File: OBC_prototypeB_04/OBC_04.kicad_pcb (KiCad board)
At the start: 2 copper layers, 95.9 x 90.2 mm, 108 parts, among them J1 PC104-8BIT, P1 3v3_IN_CONNECTOR, P10 FLASH_CS, P11 USB_5V, P12 LOAD, P13 WD_EN, P14 WD_RST_EN, P15 3pin-DC-power, P16 JTAG_10PIN, P2 INA_INPUT, P3 INA_GND, P4 INA_EN, P5 INA_OUTPUT, P6 USB_PORT, P8 RTC_SPI, P9 FLASH_SPI, Q1 DMN2075U, Q2 DMN2075U, Q3 1v2_GOOD, Q4 DMN2075U, Q5 DMN2075U, SW1 SPST, SW2 SPST, SW4 SPST, U1 TMS570LS0714, U10 FT230XQ-R, U11 STLM75, U2 XC6222B121MR-G, U3 AP7361_3.3v, U4 INA301, U5 FLASH_IS25LP016D, U6 FLASH_IS25LP016D, U7 FLASH_IS25LP016D, U8 AB-RTCMC-EOA9-S3, U9 TPS3110, Y1 XTAL

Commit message: Initial placement mostly complete
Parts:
- moved R22 159.0 mm to (68.5, 46.8)
- moved R23 159.0 mm to (68.1, 54.4)
- moved R25 148.4 mm to (73.0, 47.0)
- moved W14 142.8 mm to (89.0, 42.0)
- moved R24 131.7 mm to (71.0, 42.0)
- moved R36 130.9 mm to (70.0, 89.0)
- moved R37 130.4 mm to (68.0, 89.0)
- moved D4 127.3 mm to (73.5, 84.0)
- moved W12 127.1 mm to (78.0, 42.0)
- moved D5 126.3 mm to (70.5, 79.0)
- moved R32 125.7 mm to (66.5, 85.0)
- moved R33 125.7 mm to (69.5, 85.0)
- moved R34 125.7 mm to (66.5, 90.0)
- moved R7 123.3 mm to (158.4, 50.4)
- moved W7 119.2 mm to (153.6, 48.8)
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
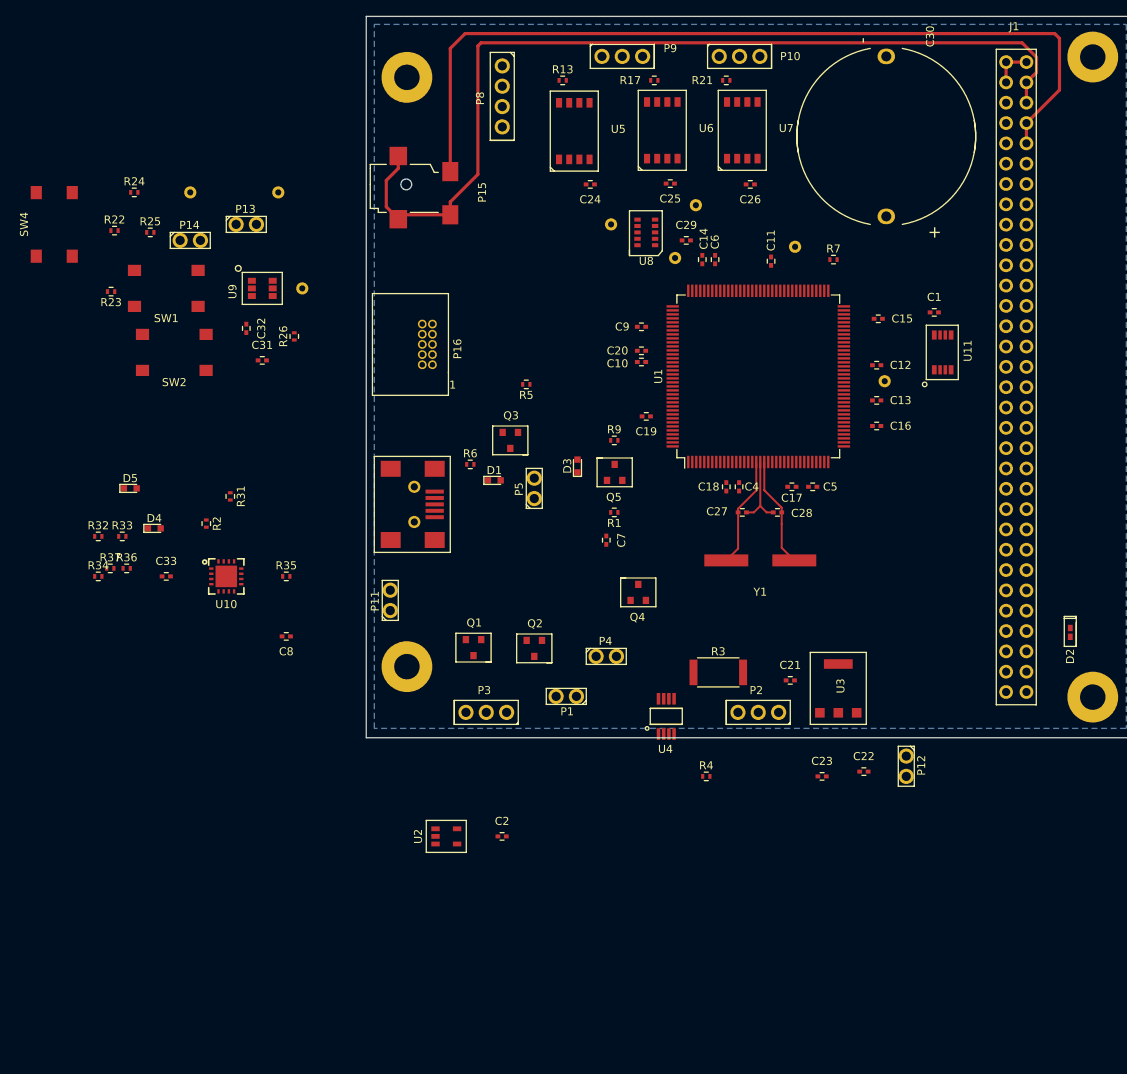
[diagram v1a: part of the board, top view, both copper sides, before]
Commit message: Routed USB, started reset area
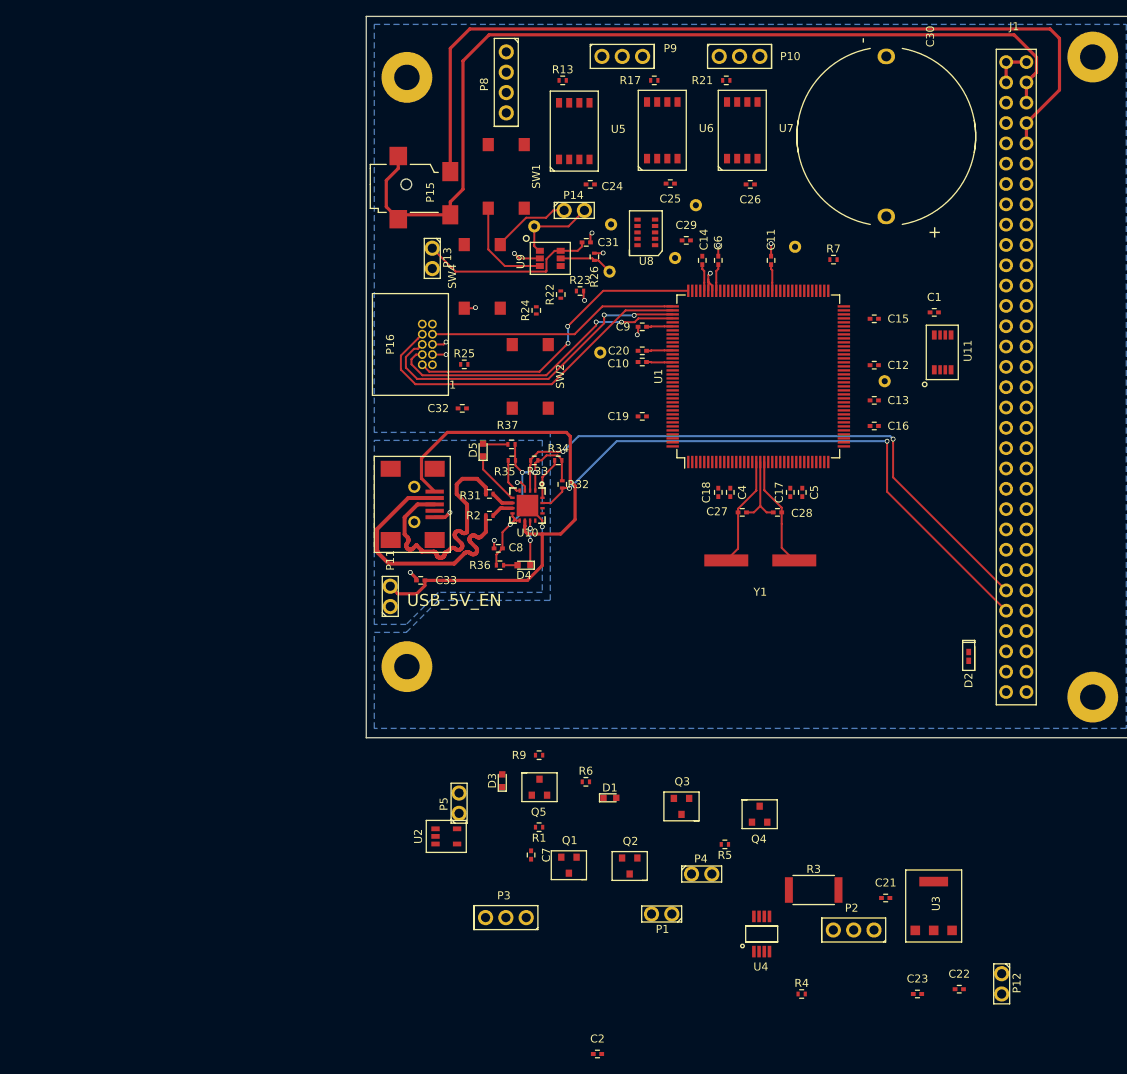
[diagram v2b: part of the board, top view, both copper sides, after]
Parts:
- moved R5 62.6 mm to (144.8, 123.5)
- moved R34 59.3 mm to (124.0, 75.5), turned to 180 degrees
- moved R23 58.6 mm to (126.7, 54.3), turned to 0 degrees
- moved R32 58.4 mm to (124.5, 78.5), turned to 270 degrees
- moved R22 56.3 mm to (124.3, 54.8), turned to 90 degrees
- moved W12 55.0 mm to (129.2, 62.0)
- moved SW4 53.9 mm to (114.5, 52.5)
- moved R37 52.5 mm to (118.2, 73.5), turned to 180 degrees
- moved R24 52.4 mm to (121.2, 56.8), turned to 90 degrees
- moved R33 52.4 mm to (121.0, 75.5), turned to 180 degrees
- moved Q3 50.5 mm to (139.4, 118.8)
- moved P14 48.1 mm to (126.0, 44.2)
- moved R36 46.7 mm to (116.7, 88.6)
- moved D4 46.4 mm to (119.7, 88.6), turned to 180 degrees
- moved SW1 44.7 mm to (117.5, 40.0), turned to 90 degrees
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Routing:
- net UART_TX: track 0.00 -> 75.3 mm, vias 0 -> 2
- net UART_RX: track 0.00 -> 73.9 mm, vias 0 -> 2
- net USB_5V: track 0.00 -> 69.3 mm
- net TDI: track 0.00 -> 44.1 mm
- net TDO: track 0.00 -> 41.9 mm, vias 0 -> 2
- net TMS: track 0.00 -> 39.1 mm, vias 0 -> 2
- net TCK: track 0.00 -> 38.7 mm, vias 0 -> 2
- net USB_P: track 0.00 -> 33.1 mm
- net USB_N: track 0.00 -> 32.2 mm
- net nTRST: track 0.00 -> 31.5 mm
- net FTDI_VCCIO: track 0.00 -> 31.0 mm, vias 0 -> 3
- net Net-(C31-Pad1): track 0.00 -> 22.6 mm
- net GND: track 0.00 -> 19.9 mm, vias 0 -> 11
- net 1v2: track 0.00 -> 13.3 mm
- net Net-(SW1-Pad1): track 0.00 -> 12.5 mm
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- added copper zone on B.Cu, net 104_In_GND
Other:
- net class USB added: clearance 0.2, trace_width 0.5, via_dia 0.6, via_drill 0.4
- net class USB_R added: clearance 0.2, trace_width 0.45, via_dia 0.6, via_drill 0.4
- board text added: "USB_5V_EN"

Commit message: Latest changes before workshop
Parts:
- moved U3 28.0 mm to (164.0, 104.0)
- moved Q4 19.6 mm to (155.0, 101.0)
- moved Q5 15.5 mm to (131.0, 104.0)
- moved Q3 14.8 mm to (139.0, 104.0)
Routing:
- net 104_GND: track 0.00 -> 1.00 mm
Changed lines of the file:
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@@
   (general
     (links 327)
-    (no_connects 305)
-    (area 56.275 19.949999 195.940001 152.045)
+    (no_connects 254)
+    (area 99.949999 19.949999 195.940001 152.045)
     (thickness 1.6)
     (drawings 5)
-    (tracks 497)
+    (tracks 499)
     (zones 0)
     (modules 108)
@@
   )
   (setup
-    (last_trace_width 0.25)
+    (last_trace_width 0.4)
     (user_trace_width 0.25)
     (user_trace_width 0.4)
@@
     (pad_to_mask_clearance 0)
     (aux_axis_origin 0 0)
-    (visible_elements FFFFFF7F)
+    (visible_elements FFFFEF7F)
     (pcbplotparams
       (layerselection 0x00030_80000001)
@@
   )
   (module SFUSat:SOT23_DMN2075U (layer F.Cu)
-    (at 139.4 118.75 180)
+    (at 139 104 180)
     (fp_text reference Q3 (at -0.1 3.1 180) (layer F.SilkS)
       (effects (font (size 1 1) (thickness 0.15)))
@@
   )
   (module SFUSat:SOT23_DMN2075U (layer F.Cu)
-    (at 149.175 119.725)
+    (at 155 101)
     (fp_text reference Q4 (at -0.1 3.1) (layer F.SilkS)
       (effects (font (size 1 1) (thickness 0.15)))
@@
   )
   (module SFUSat:SOT23_DMN2075U (layer F.Cu)
-    (at 121.65 116.35)
+    (at 131 104)
     (fp_text reference Q5 (at -0.1 3.1) (layer F.SilkS)
       (effects (font (size 1 1) (thickness 0.15)))
@@
   )
   (module SFUSat:SOT-223 (layer F.Cu)
-    (at 170.925 131.2)
+    (at 164 104.05)
     (solder_paste_ratio -0.05)
     (fp_text reference U3 (at 0.3 -0.3 90) (layer F.SilkS)
@@
   (segment (start 135.625 58.75) (end 137.275 58.75) (width 0.25) (layer F.Cu) (net 1))
   (segment (start 137.275 58.75) (end 138.3 58.75) (width 0.25) (layer F.Cu) (net 1))
+  (segment (start 131.95 104.95) (end 131.95 105) (width 0.4) (layer F.Cu) (net 2))
   (segment (start 112.25 56.475) (end 113.575 56.475) (width 0.25) (layer F.Cu) (net 2))
   (segment (start 113.575 56.475) (end 113.65 56.4) (width 0.25) (layer F.Cu) (net 2))
@@
   (segment (start 135.625 61.75) (end 137.275 61.75) (width 0.25) (layer F.Cu) (net 5))
   (segment (start 137.275 61.75) (end 138.3 61.75) (width 0.25) (layer F.Cu) (net 5))
+  (segment (start 164 107.1) (end 164 106.1) (width 0.4) (layer F.Cu) (net 7))
   (segment (start 145 88) (end 146.475 86.525) (width 0.25) (layer F.Cu) (net 9))
   (segment (start 146.475 86.525) (end 146.475 82.030952) (width 0.25) (layer F.Cu) (net 9))
@@
     (connect_pads (clearance 0.508))
     (min_thickness 0.254)
-    (fill yes (arc_segments 16) (thermal_gap 0.508) (thermal_bridge_width 0.508))
+    (fill (arc_segments 16) (thermal_gap 0.508) (thermal_bridge_width 0.508))
     (polygon
       (pts

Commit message: changes from work session - power section mostly done
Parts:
- moved C2 64.7 mm to (128.9, 85.0), turned to 180 degrees
- moved R4 51.7 mm to (119.5, 104.0), turned to 180 degrees
- moved C23 47.7 mm to (155.0, 96.5), turned to 90 degrees
- moved U4 46.9 mm to (119.0, 99.0), turned to 180 degrees
- moved P12 45.7 mm to (150.0, 106.0)
- moved U2 44.5 mm to (145.0, 95.0), turned to 0 degrees
- moved C22 41.7 mm to (161.0, 102.0), turned to 180 degrees
- moved C21 37.6 mm to (140.0, 102.0)
- moved R3 31.2 mm to (135.0, 106.0), turned to 180 degrees
- moved P1 31.2 mm to (129.0, 102.0), turned to 270 degrees
- moved R5 30.8 mm to (140.0, 93.0), turned to 270 degrees
- moved P3 29.9 mm to (124.0, 103.5), turned to 90 degrees
- moved C7 29.9 mm to (122.0, 95.0)
- moved Q1 28.9 mm to (113.0, 100.0)
- moved D3 28.8 mm to (139.0, 97.0), turned to 270 degrees
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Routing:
- net Net-(R1-Pad1): track 0.00 -> 188.8 mm
- net 5v0: track 0.00 -> 89.7 mm, vias 0 -> 4
- net 104_GND: track 1.00 -> 80.2 mm
- net 3v3: track 6.67 -> 84.6 mm
- net GND: track 20.0 -> 72.7 mm, vias 11 -> 47
- net INA_INPUT: track 0.00 -> 50.3 mm, vias 0 -> 1
- net 104_In_GND: track 14.7 -> 51.5 mm, vias 5 -> 7
- net GIOA6: track 0.00 -> 33.6 mm
- net INA_OUT: track 0.00 -> 31.1 mm
- net Net-(P4-Pad2): track 0.00 -> 29.0 mm
- net INA_ALERT: track 0.00 -> 15.0 mm
- net Net-(P1-Pad2): track 0.00 -> 15.0 mm
- net Net-(P3-Pad1): track 0.00 -> 13.1 mm, vias 0 -> 1
- net 3v3_OUTPUT: track 0.00 -> 11.6 mm
- net 1v2: track 13.3 -> 24.1 mm
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
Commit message: Routed all traces to 104 connector. Ugh
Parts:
- moved R7 59.1 mm to (124.1, 98.6)
- moved R24 11.5 mm to (128.1, 66.0)
- moved W7 2.04 mm to (151.8, 47.8)
- moved W8 1.59 mm to (166.2, 64.8)
- moved C1 0.55 mm to (171.5, 56.9)
- moved C15 0.48 mm to (163.0, 57.8)
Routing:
- net Net-(R1-Pad1): track 188.8 -> 19.9 mm
- net 104_In_GND: track 51.5 -> 155.6 mm, vias 7 -> 6
- net 5v0: track 89.7 -> 188.0 mm, vias 4 -> 2
- net I2C_SDA: track 0.00 -> 89.9 mm, vias 0 -> 2
- net MASTER_RESET: track 9.82 -> 97.3 mm, vias 0 -> 3
- net I2C_SCL: track 0.00 -> 85.4 mm, vias 0 -> 2
- net RF_GAIN_CS: track 0.00 -> 61.6 mm, vias 0 -> 4
- net GIOA0: track 0.00 -> 61.1 mm, vias 0 -> 3
- net NHET1_22: track 0.00 -> 58.5 mm, vias 0 -> 3
- net GIOA1: track 0.00 -> 58.2 mm, vias 0 -> 3
- net GIOB1: track 0.00 -> 55.7 mm, vias 0 -> 3
- net RF_CLK: track 0.00 -> 54.8 mm, vias 0 -> 1
- net RF_MISO: track 0.00 -> 54.0 mm
- net RF_PWM1: track 0.00 -> 53.9 mm, vias 0 -> 2
- net NHET1_7: track 0.00 -> 53.3 mm, vias 0 -> 1
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
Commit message: Jan 24th Joe evening
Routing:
- net GND: track 80.2 -> 457.1 mm, vias 54 -> 80
- net 3v3: track 135.8 -> 360.1 mm, vias 1 -> 28
- net 1v2: track 75.5 -> 156.8 mm, vias 2 -> 11
- net FLASH_MOSI: track 0.00 -> 76.5 mm, vias 0 -> 4
- net INA_OUT: track 37.2 -> 111.2 mm, vias 0 -> 4
- net FLASH0_CS: track 0.00 -> 71.2 mm, vias 0 -> 2
- net 104_In_GND: track 155.6 -> 222.4 mm, vias 6 -> 10
- net FLASH_MISO: track 0.00 -> 65.3 mm, vias 0 -> 2
- net RTC_CS: track 0.00 -> 64.2 mm, vias 0 -> 2
- net FLASH2_CS: track 0.00 -> 63.9 mm, vias 0 -> 4
- net FLASH_CLK: track 0.00 -> 55.4 mm, vias 0 -> 6
- net RTC_MOSI: track 0.00 -> 52.9 mm, vias 0 -> 2
- net RTC_CLK: track 0.00 -> 49.9 mm, vias 0 -> 2
- net RTC_MISO: track 0.00 -> 48.0 mm, vias 0 -> 2
- net Net-(C32-Pad1): track 0.00 -> 43.4 mm, vias 0 -> 6
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
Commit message: Fixed most DRC issues
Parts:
- moved C5 1.35 mm to (155.8, 79.5)
- moved C17 1.15 mm to (154.2, 79.4)
- moved C18 0.63 mm to (143.4, 79.5)
- moved C4 0.63 mm to (144.9, 79.5)
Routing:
- net FLASH1_CS: track 28.2 -> 74.5 mm, vias 0 -> 4
- net GND: track 457.1 -> 416.3 mm, vias 80 -> 72
- net GIOB1: track 56.8 -> 95.8 mm, vias 3 -> 4
- net (no net): track 0.00 -> 37.8 mm, vias 0 -> 4
- net RTC_CS: track 64.2 -> 90.5 mm
- net 1v2: track 156.8 -> 166.6 mm, vias 11 -> 13
- net 3v3: track 360.1 -> 353.2 mm, vias 28 -> 27
- net TDO: track 47.1 -> 43.1 mm
- net RTC_MOSI: track 52.9 -> 49.6 mm
- net Net-(C30-Pad1): track 34.2 -> 37.0 mm, vias 4 -> 3
- net RF_GAIN_CS: track 61.9 -> 64.4 mm
- net I2C_SDA: track 90.5 -> 92.9 mm
- net NHET1_22: track 56.6 -> 54.3 mm
- net I2C_SCL: track 86.0 -> 88.1 mm
- net GIOA1: track 58.6 -> 60.5 mm
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
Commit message: Apparently no unconnected :)
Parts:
- moved C20 1.90 mm to (132.7, 61.3)
- moved C10 0.43 mm to (134.1, 63.0)
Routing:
- net 3v3: track 353.2 -> 416.9 mm, vias 27 -> 28
- net (no net): track 37.8 -> 0.00 mm, vias 4 -> 0
- net 1v2: track 166.6 -> 203.3 mm, vias 13 -> 11
- net WATCHDOG: track 27.7 -> 42.4 mm, vias 4 -> 2
- net GND: track 416.3 -> 426.2 mm, vias 72 -> 63
- net NHET1_22: track 54.3 -> 57.4 mm
- net Net-(C32-Pad1): track 43.4 -> 40.9 mm
- net TMS: track 41.8 -> 39.8 mm, vias 2 -> 4
- net TDI: track 46.0 -> 44.7 mm
- net nERROR: track 11.2 -> 10.0 mm
- net INA_OUT: track 110.2 -> 110.9 mm
- net RTC_CS: track 90.5 -> 89.8 mm
- net UART_TX: track 97.5 -> 97.7 mm, vias 5 -> 7
